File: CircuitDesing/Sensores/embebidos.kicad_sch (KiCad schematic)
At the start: 0 parts

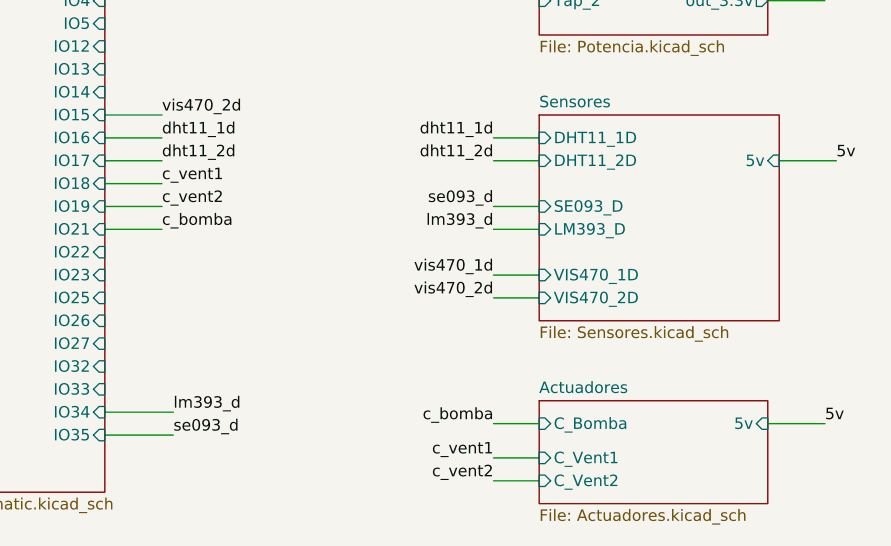
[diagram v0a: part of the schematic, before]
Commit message: Eliminado Actuadores
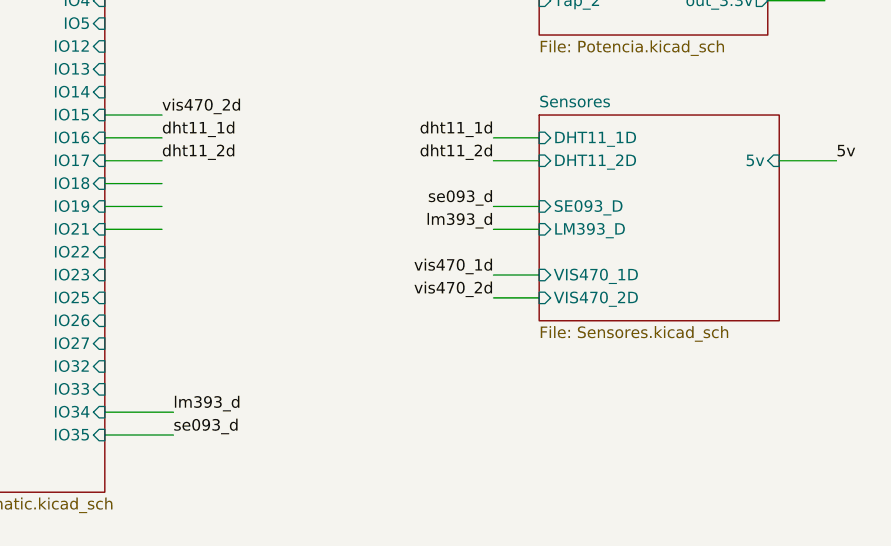
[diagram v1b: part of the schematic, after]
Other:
- removed sheet Actuadores

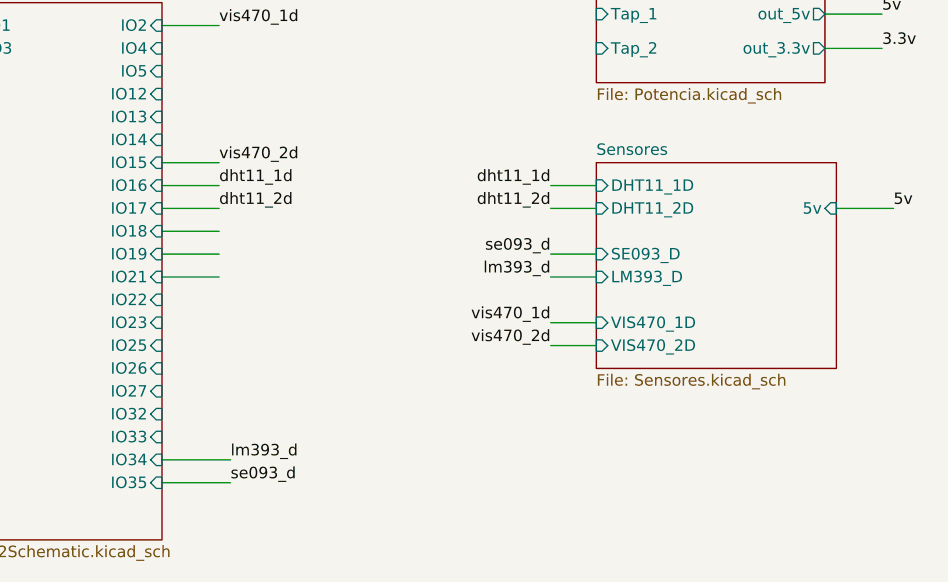
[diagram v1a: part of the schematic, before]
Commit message: Conector REED SWITCH PARA PUERTA
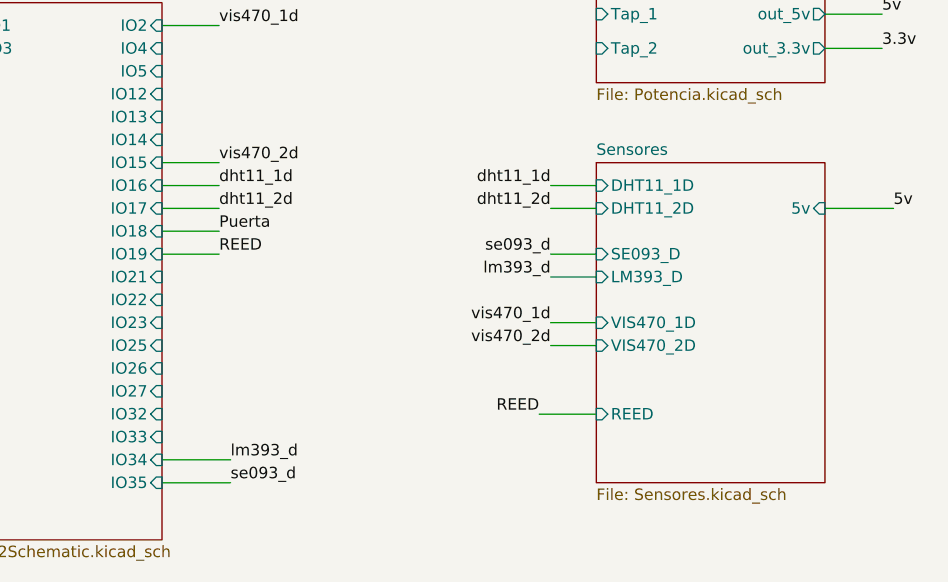
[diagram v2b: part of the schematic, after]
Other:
- sheet Sensores ports: added REED; removed none
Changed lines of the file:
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@@
+    (stroke (width 0) (type default) (color 0 0 0 0))
+  )
+  (wire (pts (xy 161.29 106.68) (xy 167.64 106.68))
     (stroke (width 0) (type default) (color 0 0 0 0))
   )
@@
     (stroke (width 0) (type default) (color 0 0 0 0))
   )
-  (wire (pts (xy 119.38 91.44) (xy 125.73 91.44))
-    (stroke (width 0) (type default) (color 0 0 0 0))
-  )
-  (wire (pts (xy 194.31 83.82) (xy 200.66 83.82))
+  (wire (pts (xy 193.04 83.82) (xy 200.66 83.82))
     (stroke (width 0) (type default) (color 0 0 0 0))
   )
@@
     (effects (font (size 1.27 1.27)) (justify left bottom))
   )
+  (label "REED" (at 125.73 88.9 0)
+    (effects (font (size 1.27 1.27)) (justify left bottom))
+  )
   (label "vis470_1d" (at 125.73 63.5 0)
     (effects (font (size 1.27 1.27)) (justify left bottom))
@@
     (effects (font (size 1.27 1.27)) (justify left bottom))
   )
+  (label "Puerta" (at 125.73 86.36 0)
+    (effects (font (size 1.27 1.27)) (justify left bottom))
+  )
   (label "vis470_2d" (at 162.56 99.06 180)
     (effects (font (size 1.27 1.27)) (justify right bottom))
@@
   (label "dht11_2d" (at 125.73 83.82 0)
     (effects (font (size 1.27 1.27)) (justify left bottom))
+  )
+  (label "REED" (at 161.29 106.68 180)
+    (effects (font (size 1.27 1.27)) (justify right bottom))
   )
   (sheet (at 92.71 60.96) (size 26.67 59.69) (fields_autoplaced)
@@
     )
   )
-  (sheet (at 167.64 78.74) (size 26.67 22.86) (fields_autoplaced)
+  (sheet (at 167.64 78.74) (size 25.4 35.56) (fields_autoplaced)
     (stroke (width 0.1524) (type solid) (color 0 0 0 0))
     (fill (color 0 0 0 0.0000))
@@
       (effects (font (size 1.27 1.27)) (justify left bottom))
     )
-    (property "Sheet file" "Sensores.kicad_sch" (id 1) (at 167.64 102.1846 0)
+    (property "Sheet file" "Sensores.kicad_sch" (id 1) (at 167.64 114.8846 0)
       (effects (font (size 1.27 1.27)) (justify left top))
     )
@@
       (effects (font (size 1.27 1.27)) (justify left))
     )
-    (pin "5v" input (at 194.31 83.82 0)
-      (effects (font (size 1.27 1.27)) (justify right))
+    (pin "5v" input (at 193.04 83.82 0)
+      (effects (font (size 1.27 1.27)) (justify right))
+    )
+    (pin "REED" input (at 167.64 106.68 180)
+      (effects (font (size 1.27 1.27)) (justify left))
     )
   )
@@
       (reference "#PWR?") (unit 1) (value "GND") (footprint "")
     )
+    (path "/4a4a8db1-1786-4804-b37e-204adf7255cc/880ea1cd-3966-42c8-a181-ad71bad43ea8"
+      (reference "#PWR?") (unit 1) (value "GND") (footprint "")
+    )
     (path "/2a66dc13-5d83-46f7-9074-3655609524a8/88b4c1f2-fa29-42b0-8b8e-d7a406d13c1c"
       (reference "#PWR?") (unit 1) (value "GND") (footprint "")
@@
       (reference "R1") (unit 1) (value "10k") (footprint "Resistor_SMD:R_0603_1608Metric_Pad0.98x0.95mm_HandSolder")
     )
+    (path "/4a4a8db1-1786-4804-b37e-204adf7255cc/bf73ab86-0883-441b-8252-73b766923c67"
+      (reference "R2") (unit 1) (value "2k") (footprint "Resistor_SMD:R_0603_1608Metric_Pad0.98x0.95mm_HandSolder")
+    )
+    (path "/4a4a8db1-1786-4804-b37e-204adf7255cc/b8ea6ad2-f255-42d0-bdd6-4a283f3cd5ee"
+      (reference "REED1") (unit 1) (value "Conn_01x02") (footprint "")
+    )
     (path "/4a4a8db1-1786-4804-b37e-204adf7255cc/52ecff1d-2404-40d4-b3d5-28684b4d8d27"

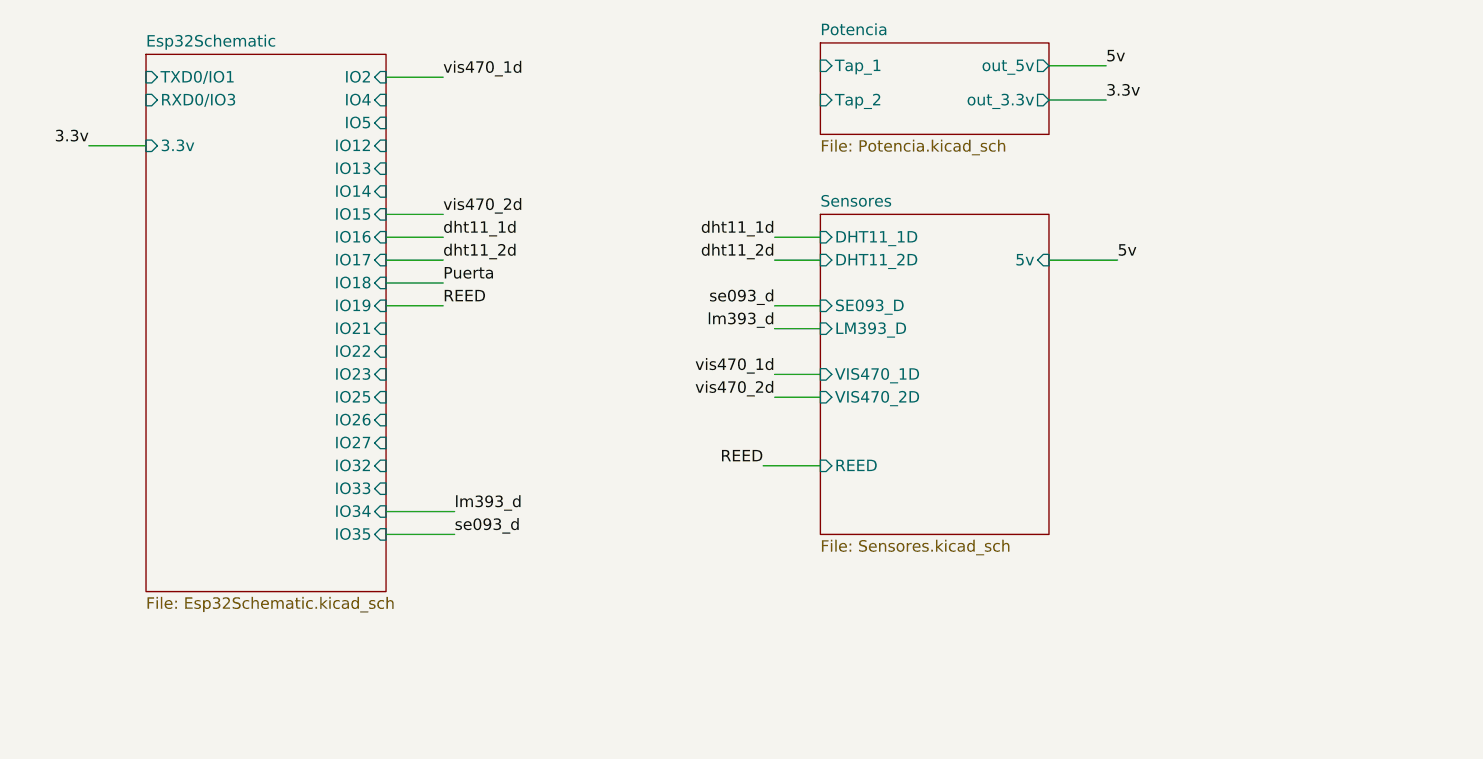
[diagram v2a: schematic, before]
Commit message: Actualizaciones de pines (Ultrasonido)
Cambios en la ubicación de pines para conexión con otros grupos.
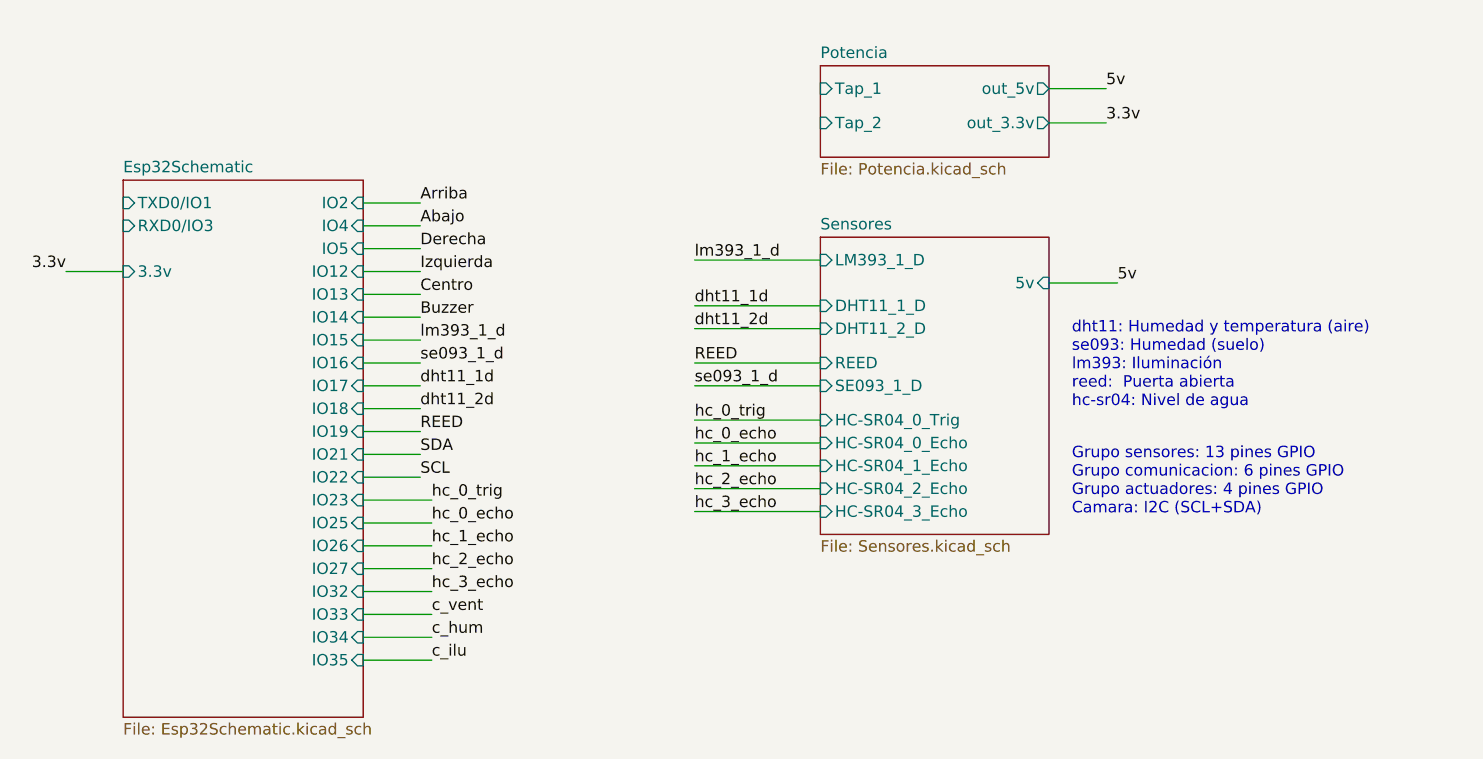
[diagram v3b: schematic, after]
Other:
- sheet Sensores ports: added DHT11_1_D, DHT11_2_D, HC-SR04_0_Echo, HC-SR04_0_Trig, HC-SR04_1_Echo, HC-SR04_2_Echo, HC-SR04_3_Echo, LM393_1_D, SE093_1_D; removed DHT11_1D, DHT11_2D, LM393_D, SE093_D, VIS470_1D, VIS470_2D
- note added: "Grupo sensores: 13 pines GPIO Grupo comunicacion: 6 pines GPIO Grupo actuadores: 4 pines GPIO Camara: I2C (SCL+SDA)"
- note added: "dht11: Humedad y temperatura (aire) se093: Humedad (suelo) lm393: Iluminación reed: Puerta abierta hc-sr04: Nivel de agua"

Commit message: UnSoloUltrasonido
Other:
- sheet Sensores ports: added none; removed HC-SR04_1_Echo, HC-SR04_2_Echo, HC-SR04_3_Echo
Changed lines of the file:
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@@
-    (stroke (width 0) (type default) (color 0 0 0 0))
-  )
-  (wire (pts (xy 153.67 111.76) (xy 167.64 111.76))
     (stroke (width 0) (type default) (color 0 0 0 0))
   )
@@
     (stroke (width 0) (type default) (color 0 0 0 0))
   )
-  (wire (pts (xy 153.67 106.68) (xy 167.64 106.68))
-    (stroke (width 0) (type default) (color 0 0 0 0))
-  )
   (wire (pts (xy 116.84 113.03) (xy 124.46 113.03))
     (stroke (width 0) (type default) (color 0 0 0 0))
@@
   )
   (wire (pts (xy 116.84 118.11) (xy 124.46 118.11))
-    (stroke (width 0) (type default) (color 0 0 0 0))
-  )
-  (wire (pts (xy 153.67 109.22) (xy 167.64 109.22))
     (stroke (width 0) (type default) (color 0 0 0 0))
   )
@@
     (effects (font (size 1.27 1.27)) (justify left bottom))
   )
-  (label "hc_2_echo" (at 124.46 118.11 0)
-    (effects (font (size 1.27 1.27)) (justify left bottom))
-  )
   (label "5v" (at 199.39 64.77 0)
     (effects (font (size 1.27 1.27)) (justify left bottom))
@@
     (effects (font (size 1.27 1.27)) (justify left bottom))
   )
-  (label "hc_3_echo" (at 153.67 111.76 0)
-    (effects (font (size 1.27 1.27)) (justify left bottom))
-  )
   (label "SCL" (at 123.19 107.95 0)
     (effects (font (size 1.27 1.27)) (justify left bottom))
@@
     (effects (font (size 1.27 1.27)) (justify left bottom))
   )
-  (label "hc_1_echo" (at 124.46 115.57 0)
-    (effects (font (size 1.27 1.27)) (justify left bottom))
-  )
   (label "hc_0_echo" (at 124.46 113.03 0)
     (effects (font (size 1.27 1.27)) (justify left bottom))
@@
     (effects (font (size 1.27 1.27)) (justify left bottom))
   )
-  (label "c_ilu" (at 124.46 128.27 0)
-    (effects (font (size 1.27 1.27)) (justify left bottom))
-  )
   (label "hc_0_trig" (at 153.67 101.6 0)
     (effects (font (size 1.27 1.27)) (justify left bottom))
@@
     (effects (font (size 1.27 1.27)) (justify left bottom))
   )
-  (label "hc_1_echo" (at 153.67 106.68 0)
-    (effects (font (size 1.27 1.27)) (justify left bottom))
-  )
   (label "c_vent" (at 124.46 123.19 0)
     (effects (font (size 1.27 1.27)) (justify left bottom))
@@
     (effects (font (size 1.27 1.27)) (justify left bottom))
   )
-  (label "hc_3_echo" (at 124.46 120.65 0)
-    (effects (font (size 1.27 1.27)) (justify left bottom))
-  )
   (label "dht11_2d" (at 123.19 100.33 0)
     (effects (font (size 1.27 1.27)) (justify left bottom))
@@
   )
   (label "se093_1_d" (at 153.67 97.79 0)
-    (effects (font (size 1.27 1.27)) (justify left bottom))
-  )
-  (label "hc_2_echo" (at 153.67 109.22 0)
     (effects (font (size 1.27 1.27)) (justify left bottom))
   )
@@
       (effects (font (size 1.27 1.27)) (justify left))
     )
-    (pin "HC-SR04_2_Echo" input (at 167.64 109.22 180)
-      (effects (font (size 1.27 1.27)) (justify left))
-    )
     (pin "DHT11_2_D" input (at 167.64 91.44 180)
       (effects (font (size 1.27 1.27)) (justify left))
@@
       (effects (font (size 1.27 1.27)) (justify left))
     )
-    (pin "HC-SR04_3_Echo" input (at 167.64 111.76 180)
-      (effects (font (size 1.27 1.27)) (justify left))
-    )
     (pin "SE093_1_D" input (at 167.64 97.79 180)
-      (effects (font (size 1.27 1.27)) (justify left))
-    )
-    (pin "HC-SR04_1_Echo" input (at 167.64 106.68 180)
       (effects (font (size 1.27 1.27)) (justify left))
     )
@@
       (reference "#PWR?") (unit 1) (value "GND") (footprint "")
     )
-    (path "/4a4a8db1-1786-4804-b37e-204adf7255cc/1625dd5a-6cbd-470c-8836-c0cd89032c60"
-      (reference "#PWR?") (unit 1) (value "GND") (footprint "")
-    )
     (path "/2a66dc13-5d83-46f7-9074-3655609524a8/a135e9bb-3dd4-4bac-8875-0b8619cdbde0/3d119db0-fa20-4eb6-83c6-89997012cb89"
       (reference "#PWR?") (unit 1) (value "GND") (footprint "")
     )
-    (path "/4a4a8db1-1786-4804-b37e-204adf7255cc/3d255b07-9e3b-4f13-9e28-2553259775c0"
-      (reference "#PWR?") (unit 1) (value "GND") (footprint "")
-    )
     (path "/4a4a8db1-1786-4804-b37e-204adf7255cc/6a843c8e-b0e6-477e-abf7-d31b7366eead"
       (reference "#PWR?") (unit 1) (value "GND") (footprint "")
@@
     )
     (path "/2a66dc13-5d83-46f7-9074-3655609524a8/74549759-895a-4805-b4eb-8b7b7d22db26/c9077a35-e1c0-4d53-8b48-cd68a78981b3"
-      (reference "#PWR?") (unit 1) (value "GND") (footprint "")
-    )
-    (path "/4a4a8db1-1786-4804-b37e-204adf7255cc/cc6fb978-ece4-4d77-b963-6de50db24c72"
       (reference "#PWR?") (unit 1) (value "GND") (footprint "")
     )
@@
       (reference "HC-SR04_0") (unit 1) (value "Conn_01x04") (footprint "")
     )
-    (path "/4a4a8db1-1786-4804-b37e-204adf7255cc/a60c507a-f76c-44d7-8b83-47470c1d67a1"
-      (reference "HC-SR04_1") (unit 1) (value "Conn_01x04") (footprint "")
-    )
-    (path "/4a4a8db1-1786-4804-b37e-204adf7255cc/b1de29a5-82e6-40aa-8cf1-5b624b93cfe8"
-      (reference "HC-SR04_2") (unit 1) (value "Conn_01x04") (footprint "")
-    )
-    (path "/4a4a8db1-1786-4804-b37e-204adf7255cc/b0d2b225-72f1-49e5-a3e8-830d42ae6284"
-      (reference "HC-SR04_3") (unit 1) (value "Conn_01x04") (footprint "")
-    )
     (path "/2a66dc13-5d83-46f7-9074-3655609524a8/a135e9bb-3dd4-4bac-8875-0b8619cdbde0/810ad703-c27e-4129-9cf8-0a0a3d8c9560"
